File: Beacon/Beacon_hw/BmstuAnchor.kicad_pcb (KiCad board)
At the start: 2 copper layers, 41 parts, among them SW1 SW_PUSH, U1 MCP1700T-3002E/TT

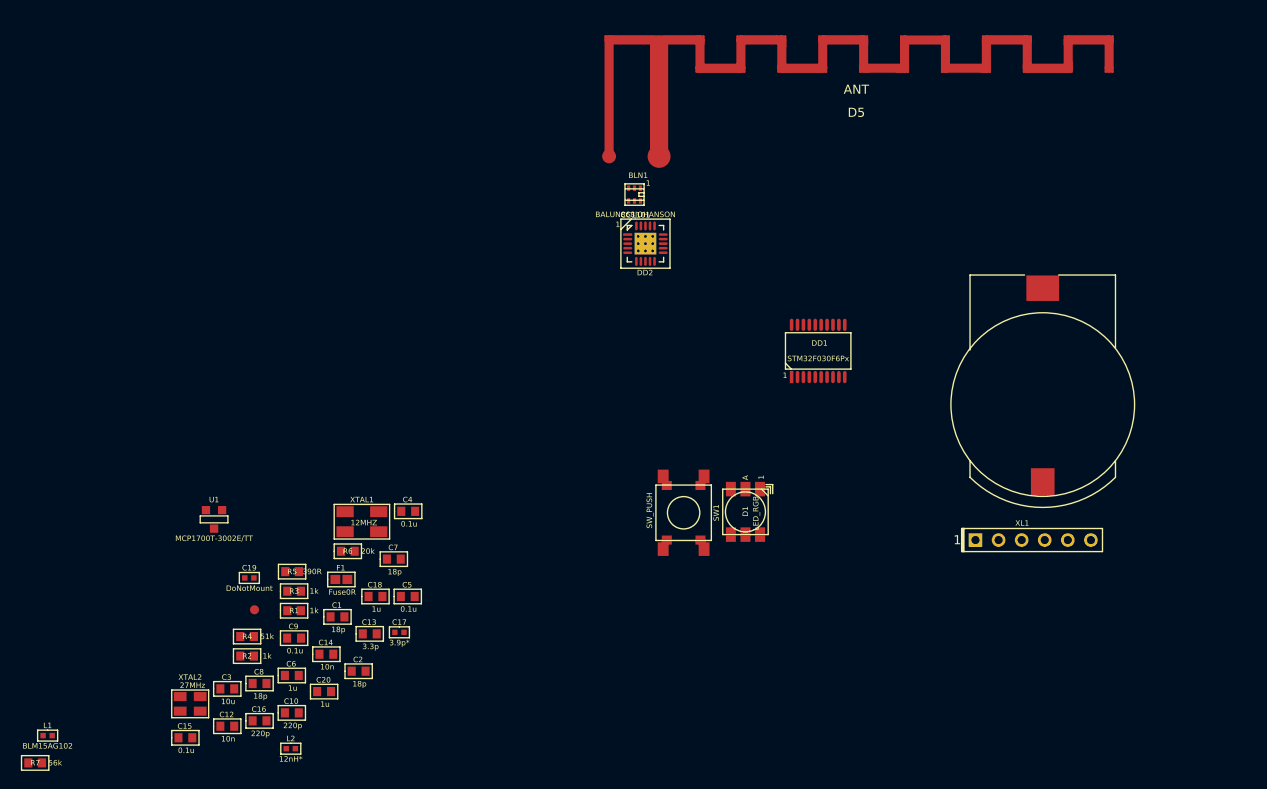
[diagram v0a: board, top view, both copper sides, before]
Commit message: +beacon pcb
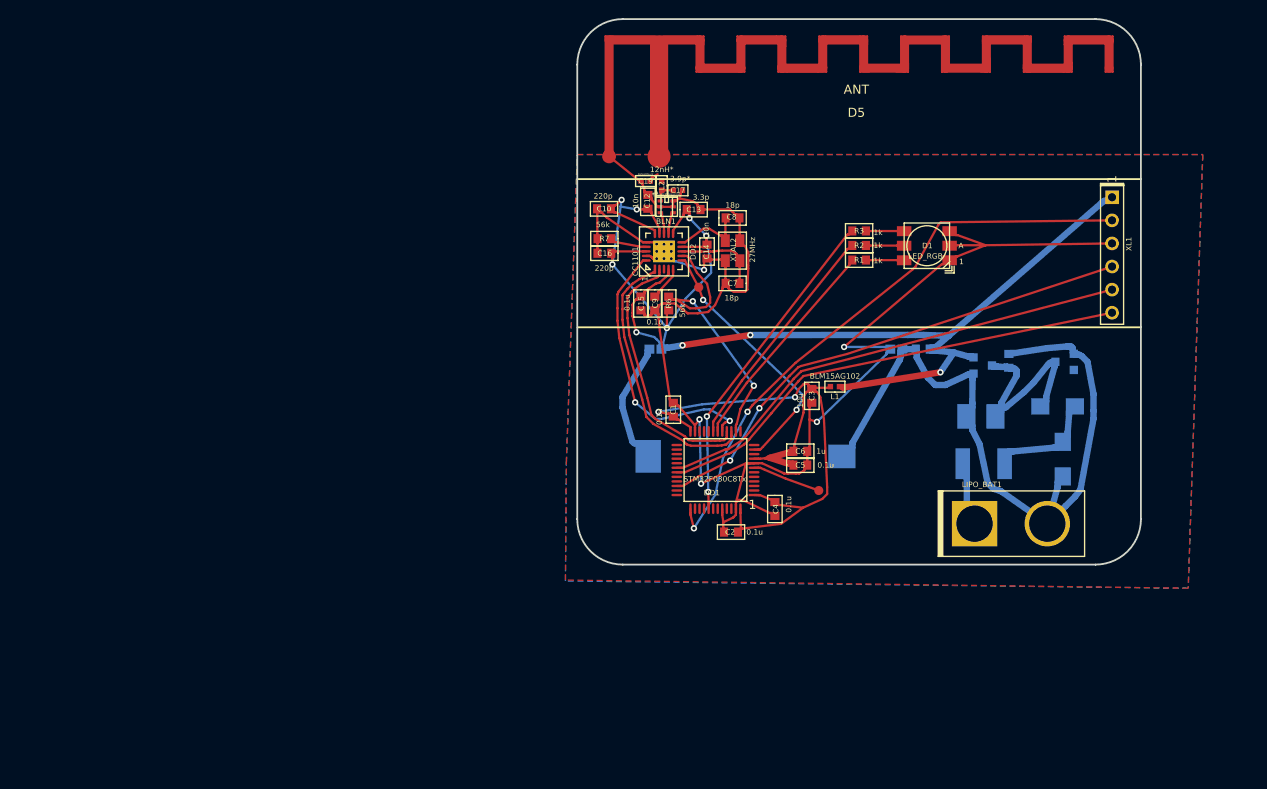
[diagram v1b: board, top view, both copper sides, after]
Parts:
- removed R4: 51k, Resistors:RES_0603
- removed R5: 390R, Resistors:RES_0603
- removed SW1: SW_PUSH, BtnsSwitches:BTN_6x6_4x4
- removed XTAL1: 12MHZ, Quartz:0503x4-4
- added C11: 0.1u 400V, Capacitors:CAP_1812, B.Cu at (144.7, 148.9)
- added C21: 100u, Capacitors:CAP_1210, B.Cu at (144.4, 143.7)
- added D2: DIODE, Diodes:SMA_DO214AC, B.Cu at (153.4, 148.4)
- added D3: DIODE, Diodes:SMA_DO214AC, B.Cu at (152.8, 142.6)
- added D4: Zener, SOT:SOT23-3, B.Cu at (153.6, 137.7)
- added F2: Fuse0R, Resistors:RES_0603_FUSE, B.Cu at (135.1, 136.3)
- added LIPO_BAT1: DW02R, Connectors:PLS-2-wide, F.Cu at (143.7, 155.5)
- added TP2: TESTPOINT, PCB:TESTPOINT_1MM, F.Cu at (126.6, 151.9)
- B1, C18, C20, F1, U1: moved to B.Cu
- C1, C2: value 18p -> 0.1u
- DD1: value STM32F030F6Px -> STM32F030C8Tx; footprint SO_DIL_TSSOP:TSSOP20 -> LQFP_TQFP:LQFP48
- R6: value 20k -> 56k
- moved L1 94.7 mm to (128.3, 140.4), turned to 180 degrees
- moved U1 86.2 mm to (144.6, 138.1), turned to 270 degrees
- moved R7 85.1 mm to (103.0, 124.2), turned to 180 degrees
- moved R2 81.1 mm to (131.0, 124.9), turned to 180 degrees
- moved XTAL2 77.7 mm to (117.1, 125.5), turned to 90 degrees
- moved C20 75.9 mm to (138.0, 136.3), turned to 180 degrees
- moved C18 74.3 mm to (147.5, 137.6), turned to 90 degrees
- moved L2 74.2 mm to (109.3, 118.3), turned to 270 degrees
- moved C12 73.9 mm to (107.8, 120.1), turned to 90 degrees
- moved R3 73.7 mm to (131.0, 123.3), turned to 180 degrees
- moved R1 73.1 mm to (131.0, 126.5), turned to 180 degrees
- moved C8 73.0 mm to (117.1, 121.9)
- moved C3 71.9 mm to (125.8, 141.4), turned to 270 degrees
- moved C15 69.2 mm to (107.0, 131.3), turned to 270 degrees
- moved C10 65.2 mm to (102.9, 120.9), turned to 180 degrees
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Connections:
- net GNDA renamed GND
- C1 pad 1: Net-(C1-Pad1) -> MCU_PWR
- C10 pad 1: +3V3 -> +3V
- C12 pad 1: +3V3 -> +3V
- C13 pad 1: +3V3 -> +3V
- C14 pad 1: +3V3 -> +3V
- C15 pad 1: +3V3 -> +3V
- C16 pad 1: +3V3 -> +3V
- C2 pad 1: Net-(C2-Pad1) -> MCU_PWR
- C20 pad 1: +3V3 -> +3V
- DD1 pad 1: GNDS -> MCU_PWR
- DD1 pad 10: /CC_CS -> Net-(DD1-Pad10)
- DD1 pad 11: /CC_SCK -> /CC_GDO0
- DD1 pad 12: /CC_MISO -> Net-(DD1-Pad12)
- DD1 pad 13: /CC_MOSI -> Net-(DD1-Pad13)
- DD1 pad 14: Net-(DD1-Pad14) -> /CC_CS
- DD1 pad 15: GNDS -> /CC_SCK
- DD1 pad 16: MCU_PWR -> /CC_MISO
- DD1 pad 17: /CC_GDO0 -> /CC_MOSI
- DD1 pad 18: /LED_B -> /LED_R
- DD1 pad 19: /SWD_IO -> /LED_G
- DD1 pad 2: Net-(C1-Pad1) -> Net-(DD1-Pad2)
- DD1 pad 20: /SWD_CLK -> Net-(DD1-Pad20)
- DD1 pad 5: MCU_PWR -> Net-(DD1-Pad5)
- DD1 pad 6: /LED_R -> Net-(DD1-Pad6)
- DD1 pad 7: /LED_G -> Net-(DD1-Pad7)
- DD1 pad 8: /UART_TX -> GNDS
- DD1 pad 9: /UART_RX -> MCU_PWR
- DD2 pad 11: +3V3 -> +3V
- DD2 pad 14: +3V3 -> +3V
- DD2 pad 15: +3V3 -> +3V
- DD2 pad 18: +3V3 -> +3V
- DD2 pad 4: +3V3 -> +3V
- DD2 pad 9: +3V3 -> +3V
- F1 pad 1: Net-(C18-Pad1) -> +3V
- L1 pad 1: +3V3 -> +3V
- R6 pad 2: +3V3 -> +3V
- U1 pad 2: +3V3 -> +3V
- XL1 pad 1: +3V3 -> +3V
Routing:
- net GNDS: track 0.00 -> 191.4 mm, vias 0 -> 5
- net +3V: track 0.00 -> 152.2 mm, vias 0 -> 10
- net GND: track 0.00 -> 79.9 mm
- net MCU_PWR: track 0.00 -> 72.7 mm, vias 0 -> 2
- net /SWD_CLK: track 0.00 -> 65.4 mm, vias 0 -> 2
- net /SWD_IO: track 0.00 -> 55.6 mm, vias 0 -> 2
- net /UART_TX: track 0.00 -> 53.2 mm
- net /UART_RX: track 0.00 -> 52.7 mm
- net /LED_B: track 0.00 -> 36.1 mm, vias 0 -> 2
- net /CC_CS: track 0.00 -> 31.4 mm, vias 0 -> 2
- net /CC_MOSI: track 0.00 -> 30.3 mm, vias 0 -> 2
- net /CC_SCK: track 0.00 -> 30.0 mm
- net Net-(C18-Pad1): track 0.00 -> 29.2 mm
- net /CC_GDO0: track 0.00 -> 28.7 mm, vias 0 -> 2
- net /CC_MISO: track 0.00 -> 28.3 mm
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- added copper zone on B.Cu, net GND
- added copper zone on F.Cu, net GNDS
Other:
- board outline added: 62 x 60 mm

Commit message: beacon pcb redraw badge fw upd
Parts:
- B1, C11, C18, C20, C21, D2, D3, D4, F1, F2, U1: moved to F.Cu
- moved XL1 65.8 mm to (103.0, 154.5), turned to 90 degrees
- moved B1 37.4 mm to (146.7, 121.3)
- moved F1 23.9 mm to (130.3, 126.3), turned to 90 degrees
- moved D1 21.4 mm to (122.0, 138.6)
- moved R3 21.0 mm to (115.4, 137.4)
- moved R1 21.0 mm to (115.4, 140.6)
- moved R2 21.0 mm to (115.4, 139.0)
- moved D3 11.5 mm to (141.4, 141.3), turned to 270 degrees
- moved D4 8.48 mm to (145.6, 140.5), turned to 270 degrees
- moved C21 8.02 mm to (151.8, 140.6), turned to 270 degrees
- moved L1 7.07 mm to (124.0, 146.0)
- moved C3 6.57 mm to (122.0, 146.8)
- moved F2 5.24 mm to (130.0, 135.1)
- moved C5 3.69 mm to (121.7, 151.5)
- moved C6 3.69 mm to (121.7, 149.9)
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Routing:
- net /SWD_CLK: track 65.4 -> 7.86 mm, vias 2 -> 0
- net /SWD_IO: track 55.6 -> 7.81 mm, vias 2 -> 0
- net /UART_TX: track 53.2 -> 10.1 mm, vias 0 -> 2
- net /UART_RX: track 52.7 -> 10.7 mm
- net GNDS: track 191.4 -> 165.6 mm, vias 5 -> 11
- net /LED_B: track 36.1 -> 18.0 mm
- net /LED_G: track 25.8 -> 7.80 mm
- net /LED_R: track 24.2 -> 6.21 mm
- net MCU_PWR: track 72.7 -> 55.6 mm, vias 2 -> 0
- net Net-(C18-Pad1): track 29.2 -> 18.4 mm
- net /CC_SCK: track 30.0 -> 20.1 mm, vias 0 -> 2
- net /CC_CS: track 31.4 -> 22.6 mm
- net /CC_MOSI: track 30.3 -> 21.6 mm
- net /CC_MISO: track 28.3 -> 19.8 mm, vias 0 -> 2
- net /BAT_+3V: track 13.7 -> 5.98 mm
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- added copper zone on B.Cu, net GNDS
- removed copper zone on B.Cu, net GND
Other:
- outline, holes or cut-outs redrawn
- rule via_min_size: 0.4 -> 0.7

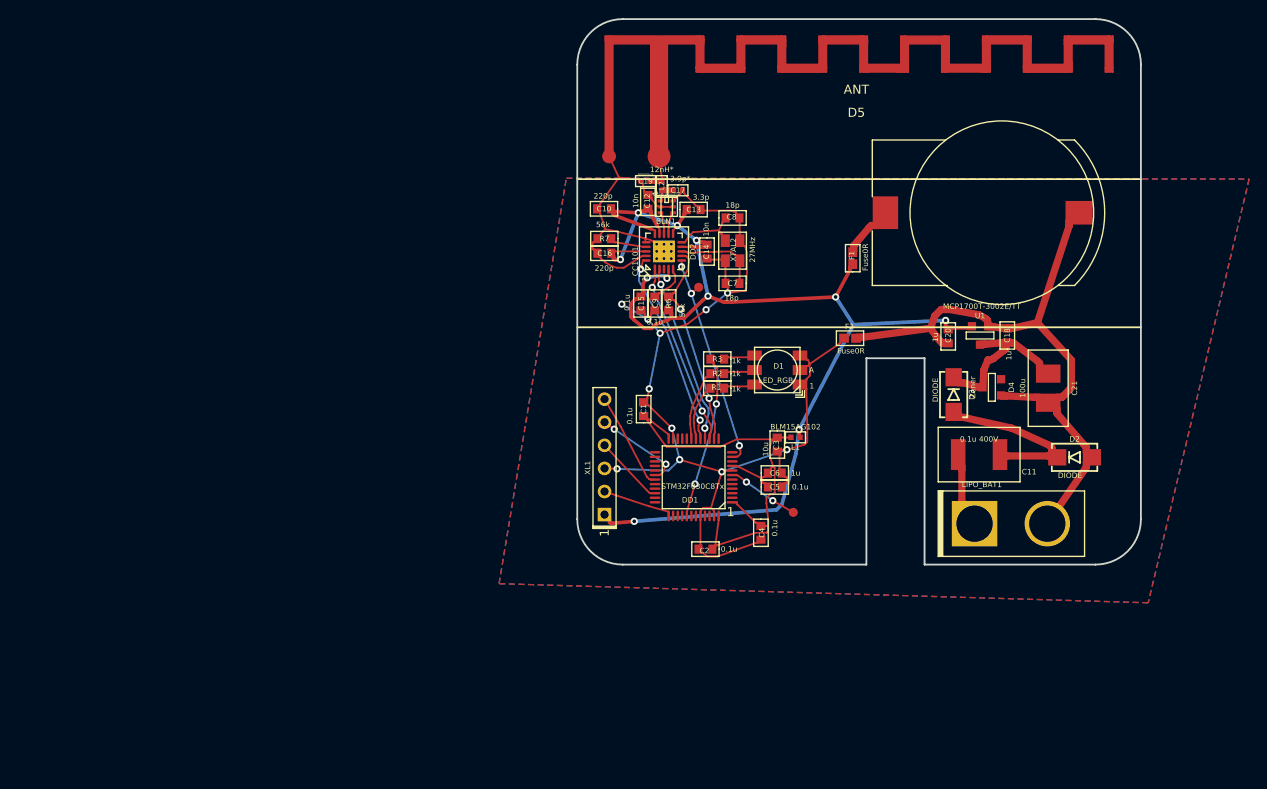
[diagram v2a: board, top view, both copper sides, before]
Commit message: *pcb upd, C before antenna added
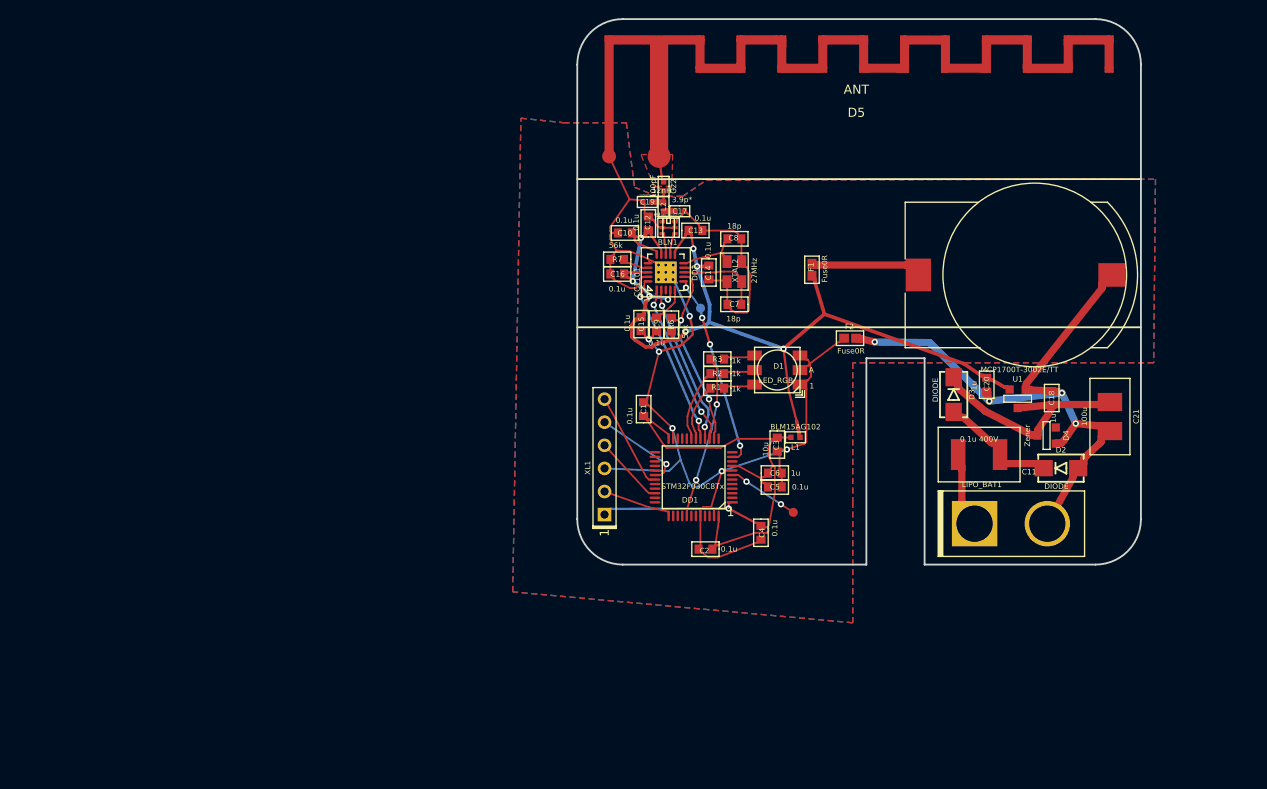
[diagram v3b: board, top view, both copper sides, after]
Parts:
- added C22: 100pF, Capacitors:CAP_0402, F.Cu at (109.5, 118.4)
- C10, C16: value 220p -> 0.1u
- C12, C14: value 10n -> 0.1u
- C13: value 3.3p -> 0.1u
- TP1: moved to B.Cu
- moved C18 8.44 mm to (152.2, 141.7)
- moved U1 8.10 mm to (148.4, 141.8)
- moved D4 8.02 mm to (151.6, 145.8)
- moved B1 7.74 mm to (150.3, 128.1)
- moved C21 7.47 mm to (158.6, 143.7)
- moved C20 6.80 mm to (145.0, 140.2)
- moved F1 4.66 mm to (125.8, 127.6)
- moved C10 3.51 mm to (105.2, 123.5)
- moved C16 2.68 mm to (104.4, 128.0)
- moved R7 2.68 mm to (104.4, 126.4)
- moved C12 2.37 mm to (107.8, 122.5)
- moved R6 2.34 mm to (110.4, 133.6)
- moved C14 2.31 mm to (114.5, 127.9)
- moved C7 2.31 mm to (117.3, 131.4)
- moved C9 2.31 mm to (108.7, 133.6)
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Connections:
- D5 pad ~: /ANT2 -> Net-(C22-Pad1)
- XL1 pad 1: +3V -> MCU_PWR
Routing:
- net +3V: track 144.8 -> 108.1 mm, vias 11 -> 8
- net MCU_PWR: track 55.6 -> 70.3 mm, vias 0 -> 1
- net Net-(C18-Pad1): track 18.4 -> 25.8 mm
- net Net-(C11-Pad1): track 19.4 -> 13.1 mm
- net /BAT_+3V: track 5.98 -> 12.3 mm
- net Net-(C22-Pad1): track 0.00 -> 2.89 mm
- net /CC_GDO0: track 24.4 -> 21.5 mm, vias 3 -> 4
- net /CC_MOSI: track 21.6 -> 19.3 mm
- net /CC_MISO: track 19.8 -> 17.6 mm
- net /CC_SCK: track 20.1 -> 18.0 mm
- net GND: track 72.3 -> 70.4 mm, vias 0 -> 4
- net GNDS: track 165.6 -> 163.7 mm, vias 11 -> 6
- net /CC_CS: track 22.6 -> 20.9 mm
- net /ANT2: track 4.02 -> 2.50 mm
- net Net-(DD2-Pad17): track 4.08 -> 2.91 mm
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- added copper zone on F.Cu, net Net-(C22-Pad1)

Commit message: AXP209 works
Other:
- rule pad_to_mask_clearance: 0.2 -> 0.1
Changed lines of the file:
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@@
-(kicad_pcb (version 20170123) (host pcbnew "(2017-02-02 revision 8dadc18)-makepkg")
+(kicad_pcb (version 20170919) (host pcbnew "(2017-09-19 revision dddaa7e69)-makepkg")
   (general
-    (links 124)
-    (no_connects 0)
-    (area 99.899999 99.899999 187.22143 160.100001)
     (thickness 1.6)
     (drawings 16)
@@
   (layers
     (0 F.Cu signal)
-    (31 B.Cu signal)
+    (31 B.Cu signal hide)
     (32 B.Adhes user)
     (33 F.Adhes user)
@@
     (pad_size 1.524 1.524)
     (pad_drill 0.762)
-    (pad_to_mask_clearance 0.2)
+    (pad_to_mask_clearance 0.1)
     (aux_axis_origin 0 0)
     (grid_origin 135.2 126.2)
@@
       (layerselection 0x00030_ffffffff)
       (usegerberextensions false)
+      (usegerberattributes true)
+      (usegerberadvancedattributes true)
+      (creategerberjobfile true)
       (excludeedgelayer true)
       (linewidth 0.100000)
@@
   (net 60 /~220V)
   (net 61 "Net-(C22-Pad1)")
-  (net_class Default "Это класс цепей по умолчанию."
+  (net_class Default "This is the default net class."
     (clearance 0.2)
     (trace_width 0.25)
